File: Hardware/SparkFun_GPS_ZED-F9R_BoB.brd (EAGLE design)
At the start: 43.2 x 50.8 mm, 138 parts, among them J1 U.FL, J3 QWIIC_RIGHT_ANGLE, J4 QWIIC_RIGHT_ANGLE, U1 HCPL-073L, U2 UBLOX_ZED_F9R, U3 UHS_INVERTER_SCHMITT_TRIGGERS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, U4 UHS_INVERTER_SCHMITT_TRIGGERS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, U5 3.3V

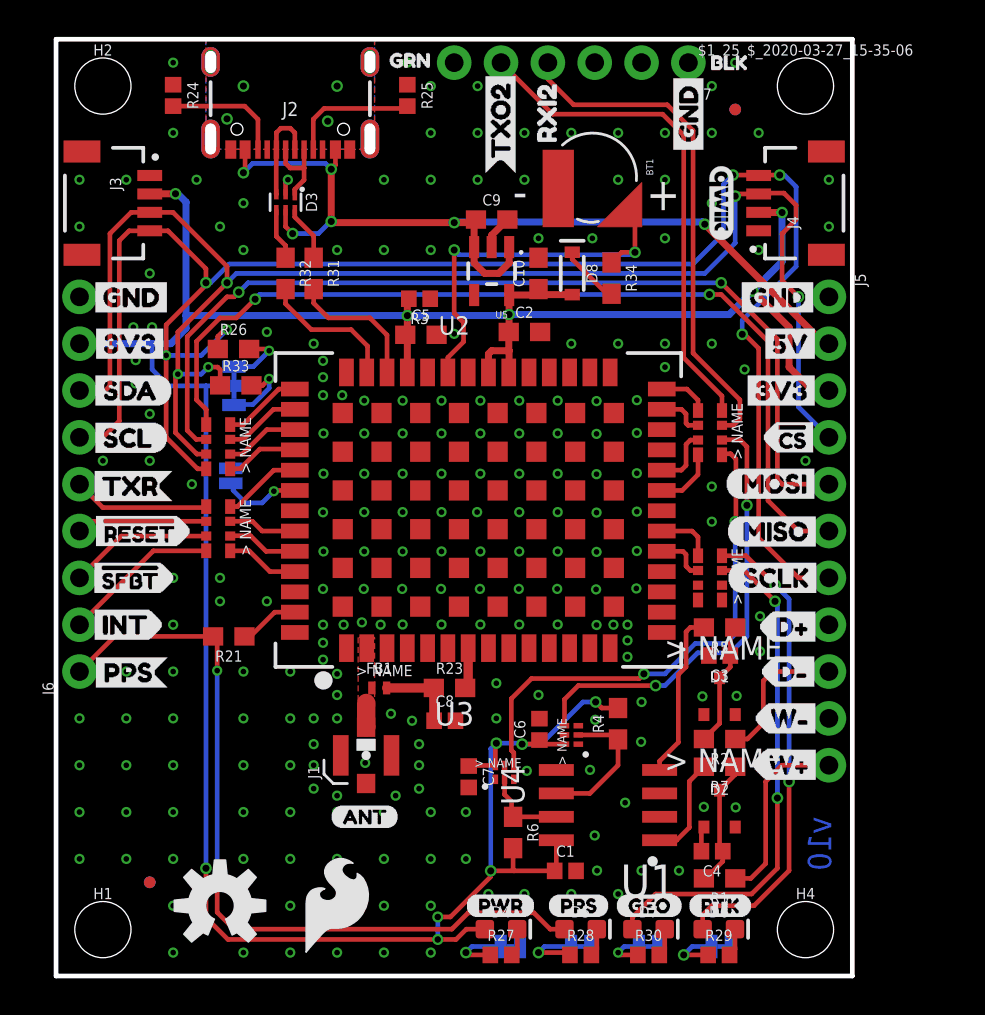
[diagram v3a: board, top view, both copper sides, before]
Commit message: Fixes packages with over sized tnames and tvalues
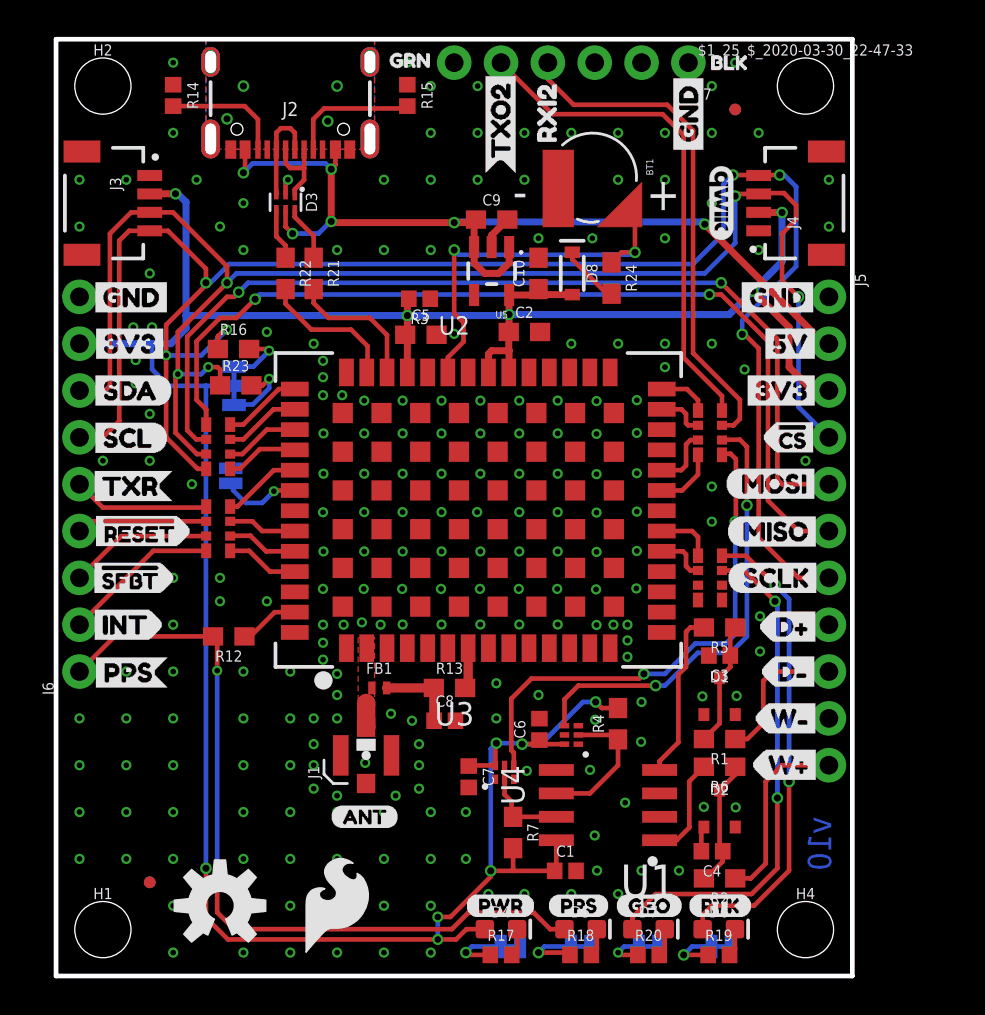
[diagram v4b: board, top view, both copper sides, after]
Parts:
- removed R31: 27, SparkFun-Resistors:0603
- removed R33: 2.2k, SparkFun-Resistors:0603
- removed R34: 3.3k, SparkFun-Resistors:0603
- added R12: 33, SparkFun-Resistors:0603
- added R14: 5.1k, SparkFun-Resistors:0402
- added R9: 33, SparkFun-Resistors:1206_RA
- R13: device SparkFun-Resistors:1206_RA -> SparkFun-Resistors:0603
- R21: value 33 -> 27
- R23: value 33 -> 2.2k
- R24: value 5.1k -> 3.3k; device SparkFun-Resistors:0402 -> SparkFun-Resistors:0603
- R6: value 910 -> 470; device classified:0603 -> SparkFun-Resistors:0603
- R7: value 470 -> 910; device SparkFun-Resistors:0603 -> classified:0603
- moved R11 26.8 mm to (35.4, 21.6)
- moved R8 26.8 mm to (8.76, 24.3)
- moved R10 26.7 mm to (35.4, 29.5)
- moved R24 25.8 mm to (30.1, 37.8)
- moved R21 20.2 mm to (14.0, 38.1), turned to 270 degrees
- moved R23 20.1 mm to (9.75, 32.0)
- moved R13 19.8 mm to (21.3, 15.6), turned to 0 degrees
- moved R6 11.7 mm to (36.0, 11.3), turned to 180 degrees
- moved R7 11.7 mm to (24.8, 7.78), turned to 270 degrees
- moved R1 7.56 mm to (36.0, 12.8)
- moved R2 7.56 mm to (36.0, 5.29)
- renumbered $1_25_$_2020-03-27_15-35-06 to $1_25_$_2020-03-30_22-47-33, GEOF to JP4, PPS to JP2, PWR to JP1, R25 to R15, R26 to R16, R27 to R17, R28 to R18, R29 to R19, R30 to R20, R32 to R22, RTK to JP3
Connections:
- net !RESET: now also R8.P2; no longer R11.P2
- net !SAFEBOOT: now also R8.P3; no longer R11.P3
- net 3.3V: now also R7.2; no longer R6.2
- net DIR+: now also R1.1; no longer R2.1
- net DIR_OUT: now also R10.P6; no longer R13.P6
- net DMINUS: now also R21.2; no longer R31.2
- net GEOF_STAT: now also R11.P7; no longer R8.P7
- net GND: now also R14.1; no longer R24.1
- net INT: now also R8.P4; no longer R11.P4
- net N$1: now also R23.2; no longer R33.2
- net N$11: now also R8.P7; no longer R11.P7
- net N$12: now also R8.P5; no longer R11.P5
- net N$14: now also R14.2; no longer R24.2
- net N$16: now also R9.P6; no longer R10.P6
- net N$17: now also R9.P5; no longer R10.P5
- net N$18: now also R8.P8; no longer R11.P8
- net N$19: now also R9.P8; no longer R10.P8
- net N$2: now also R24.2; no longer R34.2
- net N$20: now also R9.P7; no longer R10.P7
- net N$21: now also R10.P1; no longer R13.P1
- net N$26: now also R10.P2; no longer R13.P2
- net N$27: now also R11.P2; no longer R8.P2
- net N$28: now also R11.P1; no longer R8.P1
- net N$29: now also R12.1; no longer R21.1
- net N$30: now also R8.P6; no longer R11.P6
- net N$31: now also R10.P4; no longer R13.P4
- net N$32: now also R10.P3; no longer R13.P3
- net N$35: now also R2.2, R6.1; no longer R1.2, R7.1
- net N$37: now also R1.2; no longer R2.2
- net N$5: now also R13.1; no longer R23.1
- net N$9: now also R21.1; no longer R31.1
- net PPS: now also R12.2; no longer R21.2
- net RTK_STAT: now also R11.P8; no longer R8.P8
- net RXI/MOSI: now also R9.P2; no longer R10.P2
- net RXI2: now also R10.P7; no longer R13.P7
- net SCL/CLK: now also R9.P4; no longer R10.P4
- net SDA/!CS: now also R23.1, R9.P3; no longer R10.P3, R33.1
- net TXO/MISO: now also R9.P1; no longer R10.P1
- net TXO2: now also R10.P8; no longer R13.P8
- net TX_READY: now also R8.P1; no longer R11.P1
- net V_BATT: now also R24.1; no longer R34.1
- net V_RF: now also R13.2; no longer R23.2
- net WT+: now also R2.1; no longer R1.1
- net WT_IN: now also R6.2; no longer R7.2
- net WT_OUT: now also R10.P5; no longer R13.P5
- net WT_SCHMITT: now also R7.1; no longer R6.1

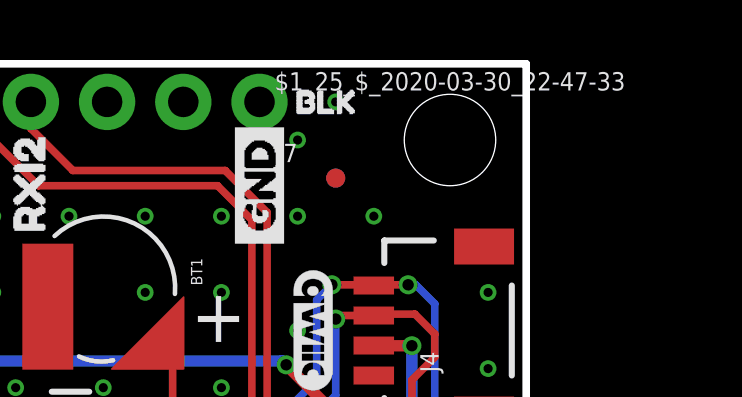
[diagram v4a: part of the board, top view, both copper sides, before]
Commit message: Fixes more tvalues and tnames
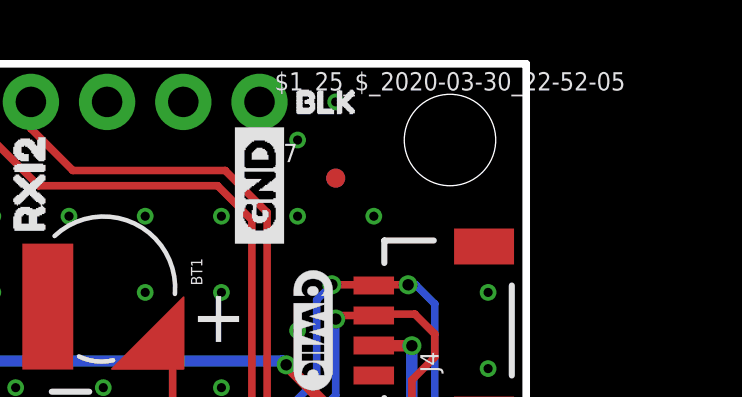
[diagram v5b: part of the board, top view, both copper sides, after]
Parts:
- renumbered $1_25_$_2020-03-30_22-47-33 to $1_25_$_2020-03-30_22-52-05

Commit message: Adds custom silk
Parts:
- removed U$52: (no value), zed:U#BLOX1
- added U$19: (no value), Dead#Reckoning#GPS#board#silk#FINAL#png:DEAD#RECKONING#GPS#BOARD#SILK#FINAL#PNG
- added U$20: (no value), Dead#Reckoning#GPS#board#silk#FINALSMALL:DEAD#RECKONING#GPS#BOARD#SILK#FINAL#PNG
- added U$25: (no value), dead reckoning:GPS_DEAD_RECKONING0
- moved U$62 39.7 mm to (20.3, 43.2)
- moved U$51 2.54 mm to (31.0, 30.4)
- moved LOGO1 0.90 mm to (9.02, 2.92)
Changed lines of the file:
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@@
 <element name="LOGO3" library="SparkFun-Aesthetics" package="SFE_LOGO_NAME_FLAME_.2" value="SFE_LOGO_NAME_FLAME.2_INCH" x="21.59" y="36.83" smashed="yes" rot="MR0"/>
 <element name="LOGO2" library="SparkFun-Aesthetics" package="QWIIC_4MM" value="QWIIC_LOGO_4MM" x="36.068" y="41.91" smashed="yes" rot="R270"/>
-<element name="LOGO1" library="SparkFun-Aesthetics" package="OSHW-LOGO-M" value="OSHW-LOGOM" x="8.89" y="3.81" smashed="yes"/>
-<element name="U$51" library="zed" package="ZED#F9R0" value="" x="30.861" y="27.813" smashed="yes" rot="MR0"/>
-<element name="U$52" library="zed" package="U#BLOX1" value="" x="29.21" y="31.242" smashed="yes" rot="MR0"/>
+<element name="LOGO1" library="SparkFun-Aesthetics" package="OSHW-LOGO-M" value="OSHW-LOGOM" x="9.017" y="2.921" smashed="yes"/>
+<element name="U$51" library="zed" package="ZED#F9R0" value="" x="30.988" y="30.353" smashed="yes" rot="MR0"/>
 <element name="U$53" library="TXR" package="GRN1" value="" x="21.082" y="49.657" smashed="yes" rot="MR0"/>
 <element name="U$54" library="TXR" package="BLK2" value="" x="38.1" y="49.53" smashed="yes" rot="MR0"/>
@@
 <attribute name="VALUE" x="19.7866" y="34.0106" size="0.6096" layer="27" font="vector" ratio="20" align="top-center"/>
 </element>
-<element name="U$62" library="SparkFun-Aesthetics" package="SFE_LOGO_FLAME_.2" value="" x="15.24" y="3.81" smashed="yes"/>
+<element name="U$62" library="SparkFun-Aesthetics" package="SFE_LOGO_FLAME_.2" value="" x="20.32" y="43.18" smashed="yes"/>
 <element name="U$67" library="Labels" package="SCL-[)" value="" x="1.651" y="29.1846" smashed="yes"/>
 <element name="U$68" library="Labels" package="SDA-[)" value="" x="1.651" y="31.75" smashed="yes"/>
@@
 <element name="R10" library="SparkFun-Resistors" package="1206_RA" value="33" x="35.433" y="29.464" smashed="yes" rot="R270"/>
 <element name="R11" library="SparkFun-Resistors" package="1206_RA" value="33" x="35.433" y="21.59" smashed="yes" rot="R270"/>
+<element name="U$19" library="Dead#Reckoning#GPS#board#silk#FINAL#png" package="DEAD#RECKONING#GPS#BOARD#SILK#FINAL#PNG" value="" x="22.098" y="22.479" smashed="yes" rot="MR0"/>
+<element name="U$20" library="Dead#Reckoning#GPS#board#silk#FINALSMALL" package="DEAD#RECKONING#GPS#BOARD#SILK#FINAL#PNG" value="" x="7.747" y="11.43" smashed="yes"/>
+<element name="U$25" library="dead reckoning" package="GPS_DEAD_RECKONING0" value="" x="32.004" y="33.274" smashed="yes" rot="MR0"/>
 </elements>
 <signals>

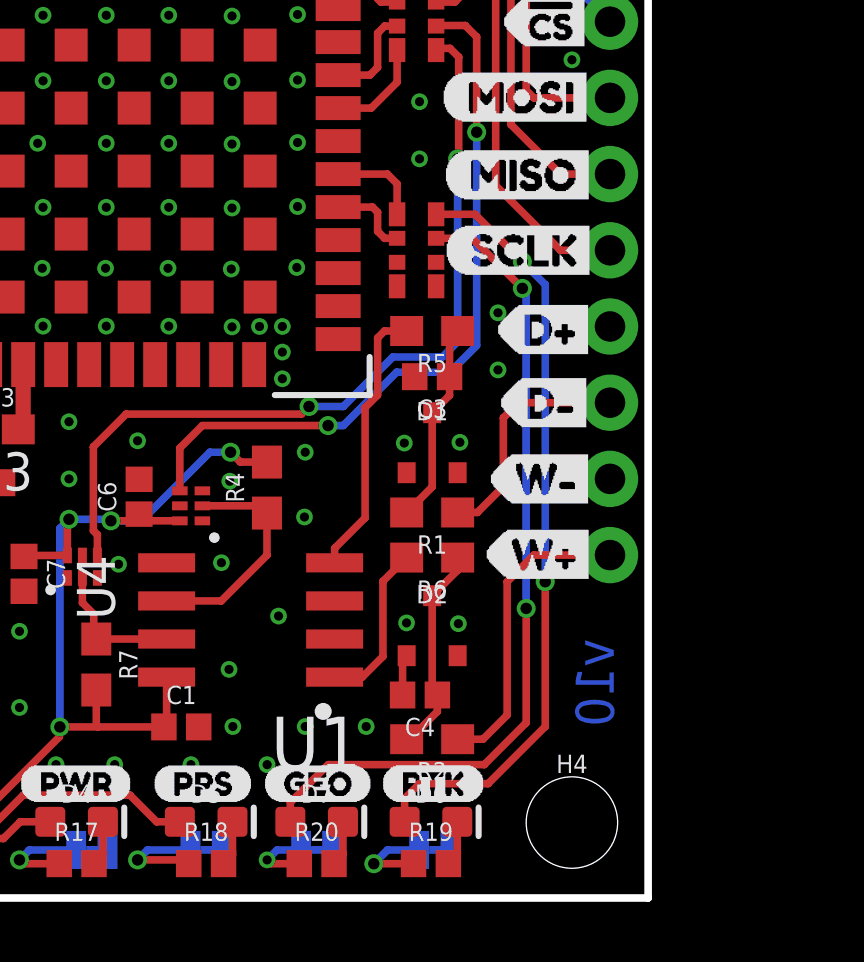
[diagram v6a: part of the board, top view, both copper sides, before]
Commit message: Updates all parts to parts in Eagle Libraries
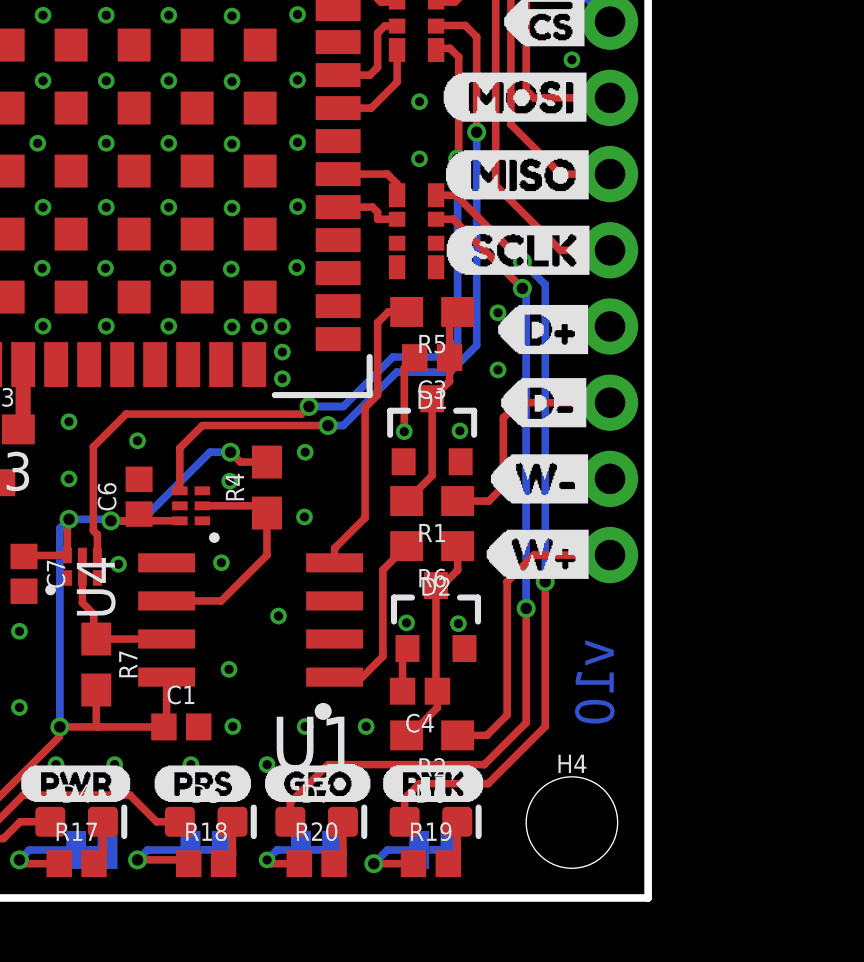
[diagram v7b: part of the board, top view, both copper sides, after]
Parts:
- D1, D2: value 0.5A/40V/420mV -> 15V; device classified:SOT23_BZX -> SparkFun-DiscreteSemi:SOT23-3
- U1: value HCPL-073L -> DUAL-OPTO_HCPL-073L; device classified:SOP_8-PIN -> SparkFun-DiscreteSemi:SOP_8-PIN
- U2: value UBLOX_ZED_F9R -> U-BLOX_ZED_F9R; device classified:UBLOX_ZED_F9R -> SparkFun-GPS:UBLOX_ZED_F9R
- U3, U4: device classified:SIP6 -> SparkFun-IC-Amplifiers:SIP6
- moved C3 0.64 mm to (36.0, 18.0)
- moved R11 0.64 mm to (35.4, 22.2)
- moved R5 0.64 mm to (36.0, 19.5)
- moved D1 0.38 mm to (36.0, 15.5)
- moved R1 0.38 mm to (36.0, 13.2)
- moved R6 0.38 mm to (36.0, 11.7)
- moved D2 0.28 mm to (36.1, 9.31)
- moved C4 0.13 mm to (35.6, 6.89)
- moved R2 0.13 mm to (36.0, 5.42)
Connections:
- net GND: now also D1.1, D2.1; no longer D1.P1, D2.P1
- net N$35: now also D2.3; no longer D2.P3
- net N$37: now also D1.3; no longer D1.P3
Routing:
- net GND: track 4.05 -> 6.79 mm
- net N$28: track 3.12 -> 2.48 mm
- net DIR_IN: track 9.15 -> 9.72 mm

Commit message: Replaces 910 Ohm resistor with part in Eagle Library
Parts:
- R4, R7: device classified:0603 -> SparkFun-Resistors:0603
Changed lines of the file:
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@@
 <attribute name="VALUE" value="15V" x="36.10855" y="9.3144" size="1.778" layer="27" display="off"/>
 </element>
-<element name="R7" library="classified" package="0603" value="910" x="24.7854" y="7.7822" smashed="yes" rot="R270">
+<element name="R7" library="SparkFun-Resistors" package="0603" value="910" x="24.7854" y="7.7822" smashed="yes" rot="R270">
 <attribute name="NAME" x="25.5474" y="7.7822" size="0.6096" layer="25" font="vector" ratio="20" rot="R270" align="bottom-center"/>
 <attribute name="PROD_ID" value="RES-13860" x="26.7854" y="28.7822" size="1.778" layer="27" font="vector" ratio="15" rot="R270" display="off"/>
 <attribute name="VALUE" x="24.0234" y="7.7822" size="0.6096" layer="27" font="vector" ratio="20" rot="R270" align="top-center"/>
 </element>
-<element name="R4" library="classified" package="0603" value="910" x="30.475" y="13.6808" smashed="yes" rot="R90">
+<element name="R4" library="SparkFun-Resistors" package="0603" value="910" x="30.475" y="13.6808" smashed="yes" rot="R90">
 <attribute name="NAME" x="29.713" y="13.6808" size="0.6096" layer="25" font="vector" ratio="20" rot="R90" align="bottom-center"/>
 <attribute name="PROD_ID" value="RES-13860" x="32.475" y="-11.3192" size="1.778" layer="27" font="vector" ratio="15" rot="R90" display="off"/>
